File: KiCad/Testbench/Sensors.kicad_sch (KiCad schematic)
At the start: 32 parts, among them J19 Conn_02x03_Counter_Clockwise, J20 Conn_02x05_Top_Bottom

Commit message: PCB before first processing
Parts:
- removed D20, D21, D22: LED, LED_SMD:LED_0805_2012Metric_Pad1.15x1.40mm_HandSolder, symbol Device:LED
- removed J19: Conn_02x03_Counter_Clockwise, Connector_Molex:Molex_Mini-Fit_Jr_5566-06A_2x03_P4.20mm_Vertical, symbol Connector_Generic:Conn_02x03_Counter_Clockwise
- removed J20: Conn_02x05_Top_Bottom, Connector_Molex:Molex_Mini-Fit_Jr_5566-10A_2x05_P4.20mm_Vertical, symbol Connector_Generic:Conn_02x05_Top_Bottom
- removed R22, R23, R31: R300, Resistor_SMD:R_1206_3216Metric_Pad1.30x1.75mm_HandSolder, symbol Device:R
- removed R24, R30: R100k, Resistor_SMD:R_1206_3216Metric_Pad1.30x1.75mm_HandSolder, symbol Device:R
- added D25, D26, D27: LED, LED_SMD:LED_0805_2012Metric_Pad1.15x1.40mm_HandSolder, symbol Device:LED
- added J19, J20, J21, J22, J23, J24, J25, J26, J27, J28: Conn_02x02_Top_Bottom, Connector_Molex:Molex_Mini-Fit_Jr_5566-04A_2x02_P4.20mm_Vertical, symbol Connector_Generic:Conn_02x02_Top_Bottom
- R25, R27, R28: value R100k -> R300
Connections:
- net 2-M2: now also R26.1, J19.1 (Pin_1), J22.3 (Pin_3)
- net 2-M3: now also J19.4 (Pin_4), J22.2 (Pin_2); no longer R25.1
- net 2-M4: now also D24.1 (K), J19.2 (Pin_2), J22.4 (Pin_4); no longer R25.2
- net 3-A1: now also R25.1, J20.1 (Pin_1), J21.3 (Pin_3)
- net 3-A2: now also D23.1 (K), J20.2 (Pin_2), J21.4 (Pin_4)
- net 3-A3: now also D25.1 (K), J23.4 (Pin_4), J25.2 (Pin_2); no longer D23.1 (K), R27.2
- net 3-A4: now also R27.1, J23.3 (Pin_3), J25.1 (Pin_1); no longer R29.1
- net 3-B1: now also J20.4 (Pin_4), J21.2 (Pin_2)
- net 3-B2: now also J23.2 (Pin_2), J25.4 (Pin_4); no longer R27.1
- net 3-B3: now also D26.1 (K), J24.2 (Pin_2), J26.4 (Pin_4); no longer R28.2
- net 3-B4: now also R28.1, J24.1 (Pin_1), J26.3 (Pin_3); no longer R26.1
- net 3-C1: now also J24.4 (Pin_4), J26.2 (Pin_2); no longer R28.1
- net 3-C2: now also J27.4 (Pin_4), J28.2 (Pin_2)
- net 3-C3: now also D27.1 (K), J27.2 (Pin_2), J28.4 (Pin_4); no longer D24.1 (K)
- net 3-C4: now also R29.1, J27.1 (Pin_1), J28.3 (Pin_3)
- net at D23.2 (A): now also R25.2; no longer R29.2
- net at D24.2 (A): now also R26.2
- new net: D27.2 (A), R29.2
- new net: D26.2 (A), R28.2
- new net: D25.2 (A), R27.2
- no-connect marks 1 -> 10
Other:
- moved on the sheet: TP34, TP35, TP36, TP37, TP38, TP39, TP40, TP41, TP42

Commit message: After work 151024
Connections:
- net 2-M2: now also J20.3 (Pin_3), R25.1; no longer J22.3 (Pin_3), R26.1
- net 2-M3: now also J20.2 (Pin_2), TP30.1; no longer J22.2 (Pin_2), TP31.1
- net 2-M4: now also D23.1 (K), J20.4 (Pin_4), TP28.1; no longer D24.1 (K), J22.4 (Pin_4), TP33.1
- net 3-A1: now also J21.1 (Pin_1), J22.3 (Pin_3), R26.1, TP32.1; no longer J20.1 (Pin_1), J21.3 (Pin_3), R25.1, TP28.1
- net 3-A2: now also D24.1 (K), J21.2 (Pin_2), J22.4 (Pin_4), TP31.1; no longer D23.1 (K), J20.2 (Pin_2), J21.4 (Pin_4), TP32.1
- net 3-A3: now also J23.2 (Pin_2), J24.4 (Pin_4), TP34.1; no longer J23.4 (Pin_4), J25.2 (Pin_2), TP35.1
- net 3-A4: now also J23.1 (Pin_1), J24.3 (Pin_3), TP35.1; no longer J23.3 (Pin_3), J25.1 (Pin_1), TP39.1
- net 3-B1: now also J21.4 (Pin_4), J22.2 (Pin_2), TP33.1; no longer J20.4 (Pin_4), J21.2 (Pin_2), TP30.1
- net 3-B2: now also J23.4 (Pin_4), J24.2 (Pin_2); no longer J23.2 (Pin_2), J25.4 (Pin_4)
- net 3-B3: now also J25.2 (Pin_2), TP37.1; no longer J24.2 (Pin_2), TP38.1
- net 3-B4: now also J25.1 (Pin_1), TP38.1; no longer J24.1 (Pin_1), TP34.1
- net 3-C1: now also J25.4 (Pin_4), TP39.1; no longer J24.4 (Pin_4), TP37.1
- net 3-C2: now also TP42.1; no longer TP41.1
- net 3-C4: now also TP41.1; no longer TP42.1
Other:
- note added: "Brake Pressure 0 (BP0)"
- note added: "Brake Pressure 1 (BP1)"
- note added: "Steering Wheel (SW)"
- note removed: "BP0"
- note removed: "BP1"
- note removed: "SW"
- note removed: "TP0"
- note removed: "TP1"

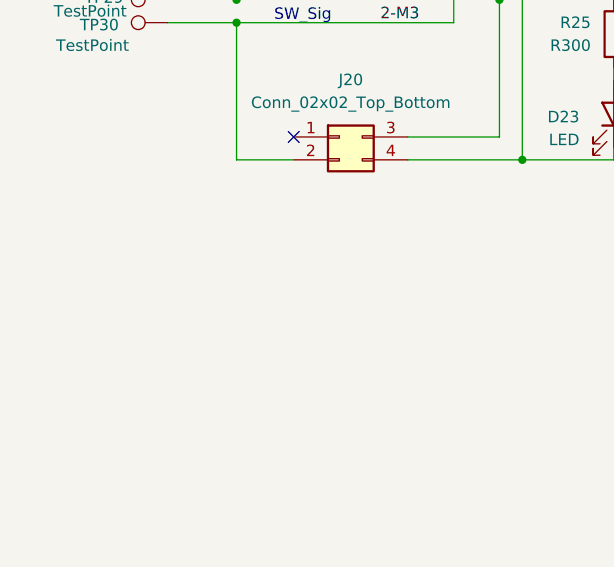
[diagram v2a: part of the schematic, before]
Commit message: Updated for PCBV2 Updated size and added LED.
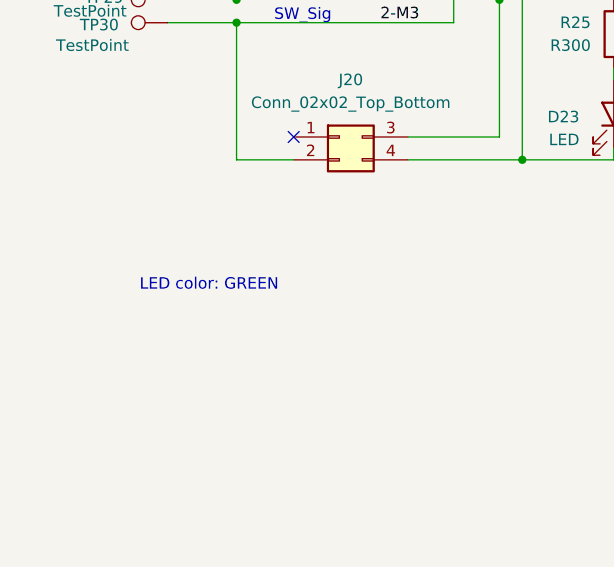
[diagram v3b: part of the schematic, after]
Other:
- note added: "LED color: GREEN"
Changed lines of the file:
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@@
+		)
+	)
+	(text "LED color: GREEN"
+		(exclude_from_sim no)
+		(at 31.242 82.55 0)
+		(effects
+			(font
+				(size 1.27 1.27)
+			)
 		)
 	)
